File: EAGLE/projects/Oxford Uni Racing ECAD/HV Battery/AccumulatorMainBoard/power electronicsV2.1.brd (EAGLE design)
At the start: 160 x 100 mm, 97 parts, among them IC1 4043D, IC2 SE555D, IC3 4011D, IC5 4043D, IC6 4011D, IC7 4011D, IC8 4011D, IC9 4011D, K1 T9AS1D12-48=T9A, K2 T9AS5D12-12=T9A, K3 T9AS1D12-48=T9A, K4 T9AS1D12-48=T9A, Q1 BSS138, Q2 BSS138, Q3 BSS138, Q4 BSS138

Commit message: New Main board
4 layer design, work in progress
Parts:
- moved TP11 319.7 mm to (34.0, 102.9)
- moved TP14 316.7 mm to (63.5, 74.9)
- moved TP3 309.1 mm to (30.5, 102.9)
- moved TP6 301.9 mm to (39.4, 83.8)
- moved LED8 297.4 mm to (54.6, 83.8), turned to 180 degrees
- moved R15 290.3 mm to (48.3, 83.8), turned to 180 degrees
- moved TP2 287.2 mm to (39.4, 76.2)
- moved TP12 284.7 mm to (45.7, 102.9)
- moved TP4 282.9 mm to (69.8, 83.8)
- moved TP23 273.5 mm to (78.7, 72.4)
- moved LED7 264.0 mm to (14.0, 81.3), turned to 180 degrees
- moved R12 263.1 mm to (19.1, 86.4)
- moved R14 258.3 mm to (10.2, 81.3), turned to 180 degrees
- moved BMS_I/O 258.3 mm to (132.1, 34.3), turned to 270 degrees
- moved TP16 249.8 mm to (37.3, 102.9)
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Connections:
- removed net N$30: IC6.12, IC6.13
- net N$9: now also IC6.12, IC6.13
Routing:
- net +12V: track 0.00 -> 192.8 mm
- net +3V3: track 0.00 -> 127.8 mm
- net GND: track 0.00 -> 119.6 mm
- net DISCHARGE_ENABLE: track 0.00 -> 68.1 mm
- net READY_POWER: track 0.00 -> 67.2 mm
- net STARTUP_RESET: track 0.00 -> 60.9 mm, vias 0 -> 3
- net N$21: track 0.00 -> 58.3 mm
- net OK_HS: track 0.00 -> 54.8 mm
- net FAN+: track 0.00 -> 53.9 mm
- net N$13: track 0.00 -> 53.3 mm
- net CAN2_L: track 0.00 -> 34.1 mm
- net N$9: track 0.00 -> 34.0 mm
- net IMD_COIL_OUT: track 0.00 -> 33.6 mm
- net CAN2_H: track 0.00 -> 33.2 mm
- net N$5: track 0.00 -> 33.0 mm, vias 0 -> 2
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- added copper zone on layer 2, net GND
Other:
- board size 160 x 100 mm -> 203.2 x 149.5 mm

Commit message: Main Board - Version 2.1
Correct dimensions, connectors placed
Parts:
- THERAL_EX_I/O, WIFI_I/O: value T821108A1S100CEU -> T816108A1S102CEU; device SamacSys_Parts:HDRV8W64P254_2X4_1778X895X915P -> T816108A1S102CEU:T816108A1S102CEU
- moved H4 237.7 mm to (160.3, 5.04), turned to 90 degrees
- moved H3 197.8 mm to (160.5, 99.3)
- moved CAN1 165.8 mm to (143.5, 24.1)
- moved WIFI_I/O 145.5 mm to (20.3, 15.2), turned to 90 degrees
- moved ISOMETER_I/O 128.9 mm to (129.5, 5.08), turned to 0 degrees
- moved H2 123.7 mm to (6.68, 6.60)
- moved MISC_I/O 72.4 mm to (7.62, 43.2), turned to 90 degrees
- moved PRECHARGE/AIRS 61.4 mm to (153.7, 91.4), turned to 141.3 degrees
- moved EMSDC 42.4 mm to (127.0, 97.8), turned to 180 degrees
- moved BMS_I/O 39.7 mm to (157.5, 64.8)
- moved H1 36.9 mm to (6.35, 97.8), turned to 90 degrees
- moved THERAL_EX_I/O 24.4 mm to (22.9, 95.2), turned to 226.4 degrees
- moved TP10 24.3 mm to (35.6, 96.5)
- moved FAN 24.1 mm to (34.3, 8.89)
- moved BMS_POWER/GND 22.9 mm to (141.0, 58.4)
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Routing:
- net CAN2_H: track 33.2 -> 287.8 mm, vias 0 -> 1
- net CAN2_L: track 34.1 -> 284.4 mm, vias 0 -> 2
- net CHASSIS_GND: track 0.00 -> 169.6 mm
- net CHARGE_SAFE: track 16.8 -> 140.8 mm, vias 0 -> 3
- net FAN_ENABLE: track 17.2 -> 133.2 mm, vias 0 -> 2
- net N$12: track 0.00 -> 113.3 mm
- net DISCHARGE_ENABLE: track 68.1 -> 175.7 mm, vias 0 -> 1
- net IMD_LED-: track 0.00 -> 97.3 mm, vias 0 -> 2
- net N$3: track 7.40 -> 98.5 mm, vias 0 -> 1
- net PRECHARGE_SELECT: track 20.8 -> 97.8 mm, vias 0 -> 1
- net READY_POWER: track 67.2 -> 8.65 mm
- net OK_HS: track 54.8 -> 8.99 mm
- net AMS_LED-: track 0.00 -> 43.1 mm, vias 0 -> 2
- net CAN1_H: track 0.00 -> 36.9 mm
- net N$2: track 31.4 -> 1.27 mm
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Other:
- board size 203.2 x 149.5 mm -> 167.6 x 103.8 mm

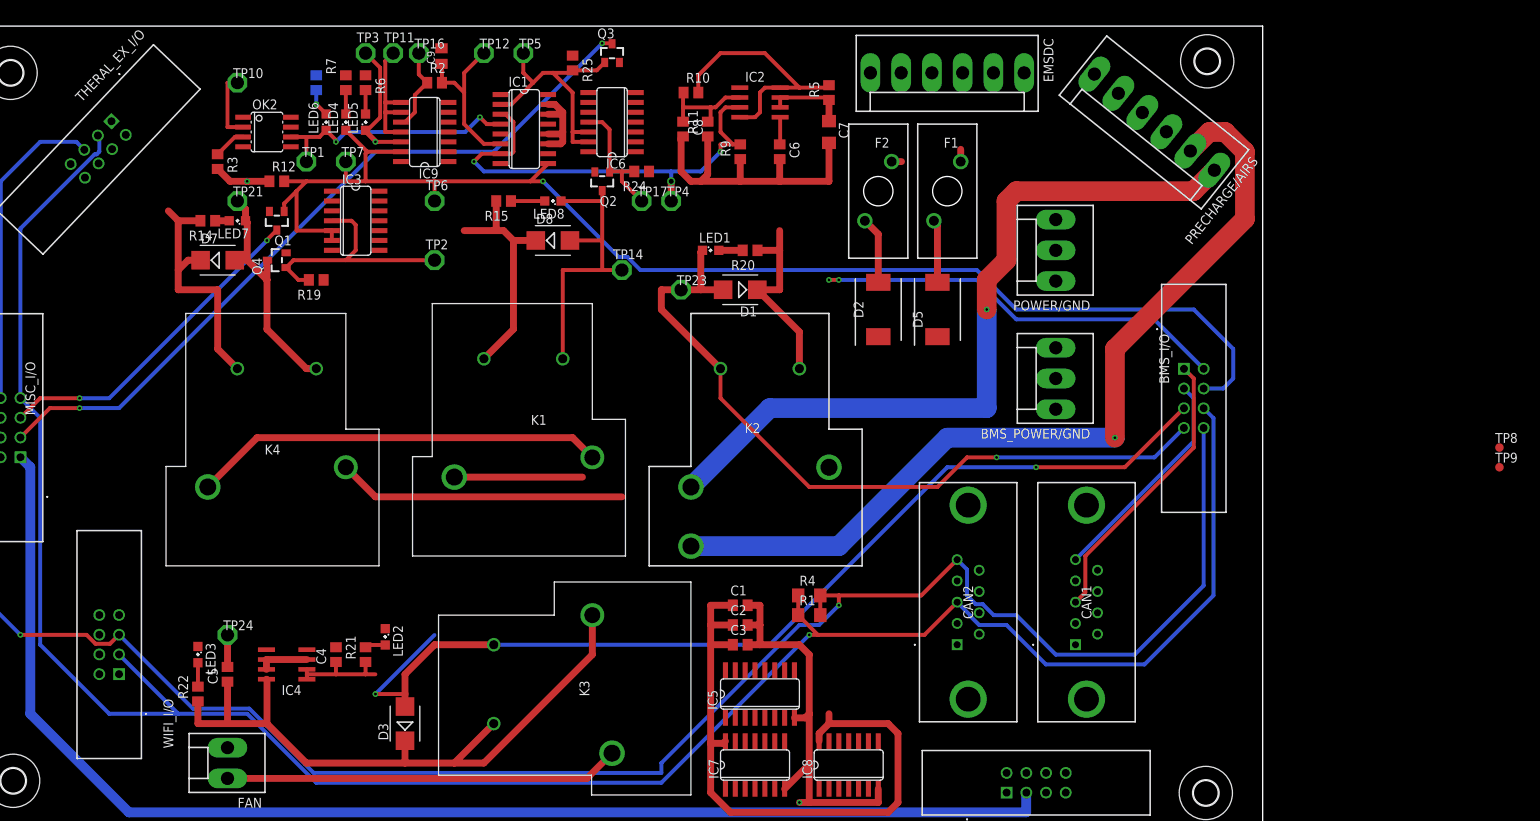
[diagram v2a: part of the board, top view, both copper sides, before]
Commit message: Main Board V2.2
Adds power plane, connects. WIP.
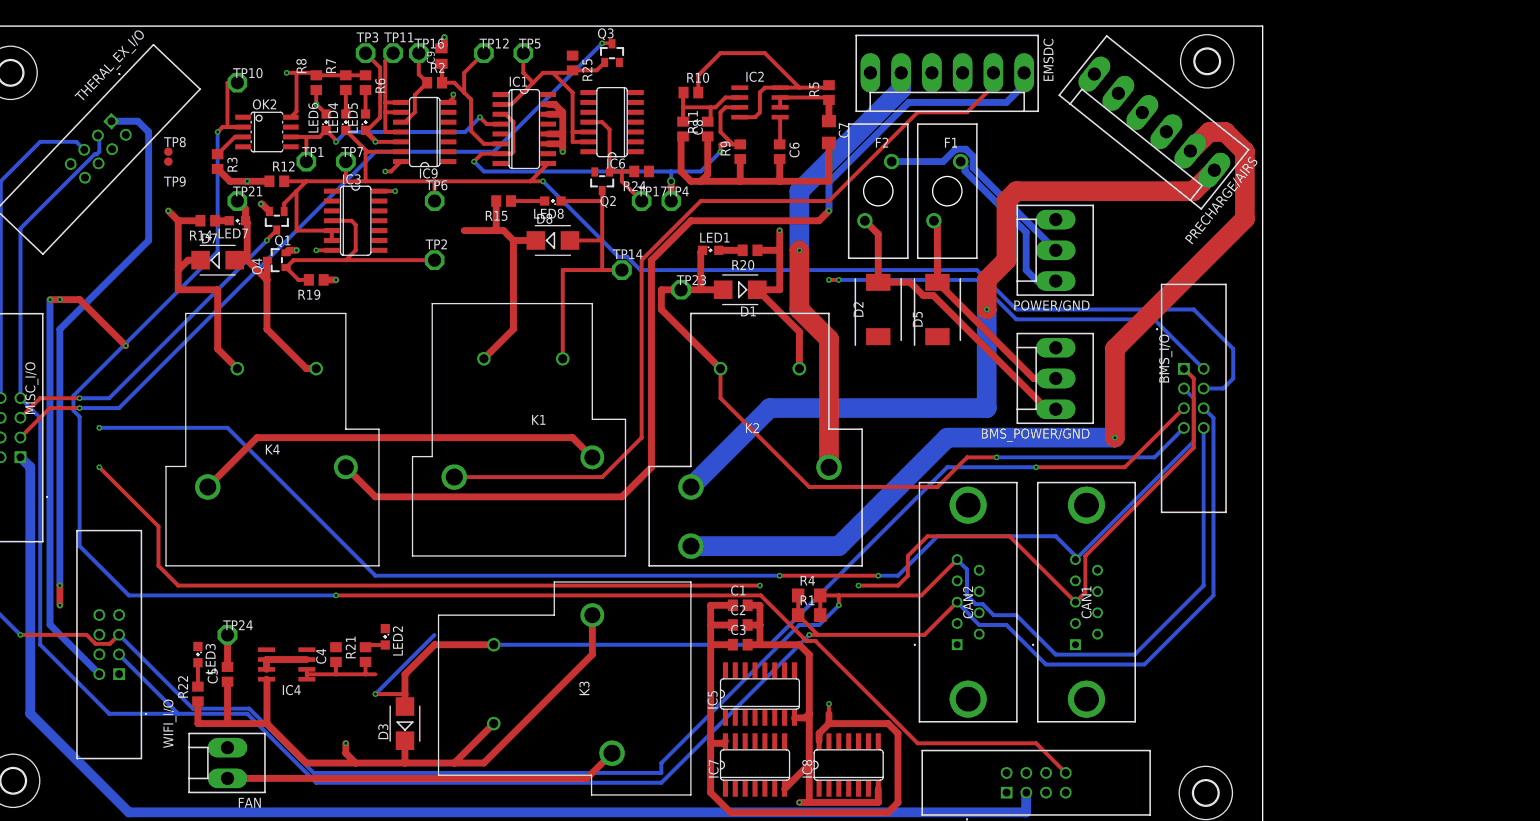
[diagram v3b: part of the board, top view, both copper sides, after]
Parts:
- moved TP9 175.9 mm to (26.7, 86.4)
- moved TP8 175.6 mm to (26.7, 87.6)
- flipped R8 to the top
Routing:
- net CHARGE_POWER: track 11.9 -> 254.9 mm, vias 0 -> 3
- net READY_POWER: track 8.65 -> 232.8 mm, vias 0 -> 2
- net OK_HS: track 8.99 -> 213.0 mm, vias 0 -> 2
- net CAN1_H: track 36.9 -> 193.9 mm, vias 0 -> 3
- net CAN1_L: track 28.9 -> 180.3 mm, vias 0 -> 3
- net N$11: track 0.00 -> 97.2 mm, vias 0 -> 1
- net N$13: track 37.1 -> 130.4 mm, vias 0 -> 1
- net N$14: track 16.5 -> 105.4 mm
- net N$2: track 1.27 -> 28.0 mm
- net N$4: track 1.58 -> 21.9 mm
- net +3V3: track 129.0 -> 146.6 mm, vias 0 -> 2
- net LOWEST_TEMP: track 0.00 -> 9.09 mm
- net HIGHEST_TEMP: track 0.00 -> 7.38 mm
- net GND: track 125.3 -> 132.5 mm, vias 2 -> 7
- net VDD: track 0.00 -> 4.54 mm, vias 0 -> 2
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- added copper zone on layer 15, net +12V
- added copper zone on layer 15, net +3V3

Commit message: Main Board V2.3
first complete main board
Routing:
- net VSS: track 3.15 -> 89.6 mm, vias 2 -> 4
- net VDD: track 4.54 -> 88.1 mm, vias 2 -> 4
- net GND: track 132.5 -> 168.3 mm, vias 7 -> 14
- net +3V3: track 146.6 -> 180.9 mm, vias 2 -> 6
- net FAN_ENABLE: track 133.2 -> 118.7 mm, vias 2 -> 1
- net +12V: track 180.4 -> 191.9 mm, vias 3 -> 4
- net CHARGE_POWER: track 254.9 -> 250.3 mm
- net CHARGE_SAFE: track 140.8 -> 139.0 mm
- net N$1: track 11.1 -> 11.8 mm
- net N$10: track 21.8 -> 22.4 mm
